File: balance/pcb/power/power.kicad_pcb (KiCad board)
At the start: 2 copper layers, 0 parts

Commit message: balance robot: power board
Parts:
- added A1: Pololu_Breakout_DRV8825, Module:Pololu_Breakout-16_15.2x20.3mm, F.Cu at (118.7, 53.6)
- added A2: Pololu_Breakout_DRV8825, Module:Pololu_Breakout-16_15.2x20.3mm, F.Cu at (181.3, 71.4)
- added J1: xt60, Connector_PinHeader_2.54mm:PinHeader_1x02_P2.54mm_Vertical, F.Cu at (148.7, 70.0)
- added J2: Conn_01x10_Male, Connector_PinHeader_2.54mm:PinHeader_1x10_P2.54mm_Vertical, F.Cu at (161.4, 55.0)
- added J3: Conn_01x04_Male, Connector_PinHeader_2.54mm:PinHeader_1x04_P2.54mm_Vertical, F.Cu at (110.0, 66.3)
- added J4: Conn_01x04_Male, Connector_PinHeader_2.54mm:PinHeader_1x04_P2.54mm_Vertical, F.Cu at (190.0, 58.7)
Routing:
- net /rb2: track 0.00 -> 8.65 mm
- net /rb1: track 0.00 -> 8.65 mm
- net /ra2: track 0.00 -> 8.65 mm
- net /ra1: track 0.00 -> 8.65 mm
- net /lb2: track 0.00 -> 8.65 mm
- net /lb1: track 0.00 -> 8.65 mm
- net /la2: track 0.00 -> 8.65 mm
- net /la1: track 0.00 -> 8.65 mm
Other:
- board outline added: 100 x 25 mm

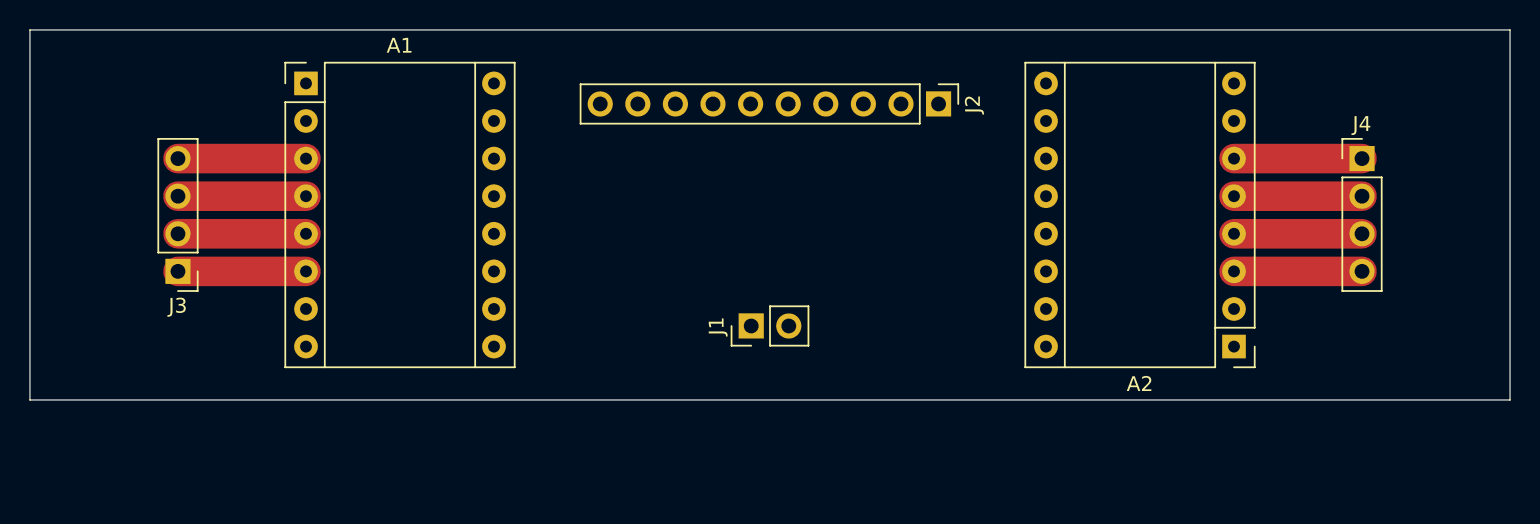
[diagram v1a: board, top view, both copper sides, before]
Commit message: balance robot: power board
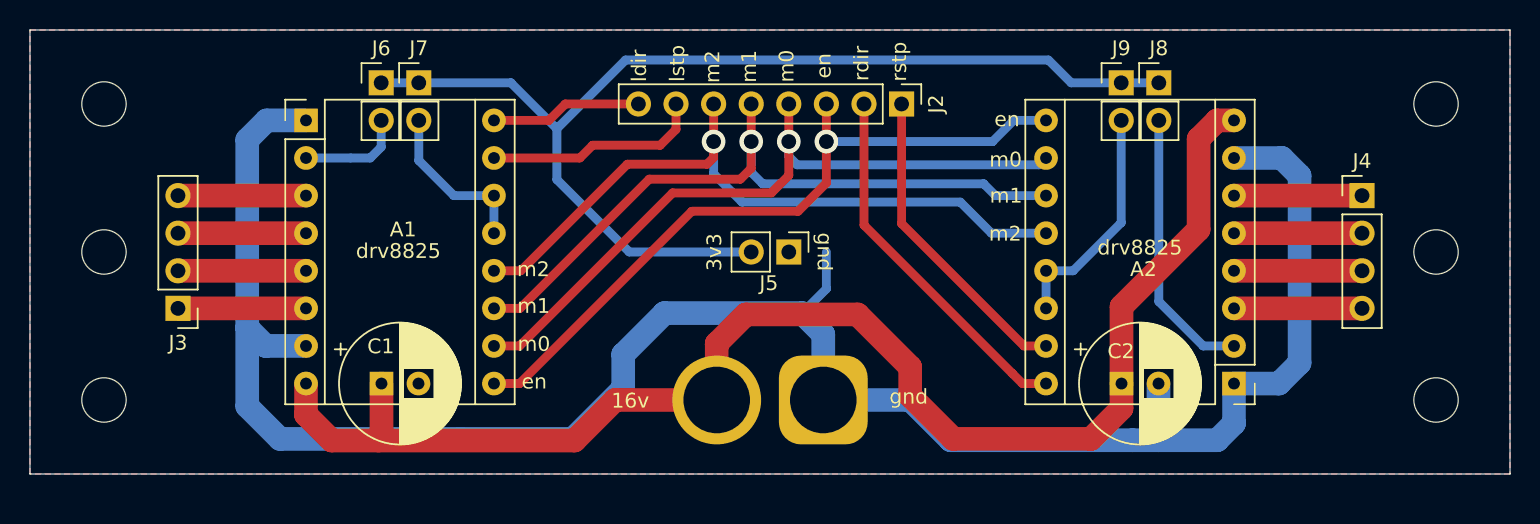
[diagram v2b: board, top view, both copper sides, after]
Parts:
- added C1: C, Capacitor_THT:CP_Radial_D8.0mm_P2.50mm, F.Cu at (123.8, 73.9)
- added C2: C, Capacitor_THT:CP_Radial_D8.0mm_P2.50mm, F.Cu at (173.8, 73.9)
- added J5: Conn_01x02_Male, Connector_PinHeader_2.54mm:PinHeader_1x02_P2.54mm_Vertical, F.Cu at (151.3, 65.0)
- added J6: Conn_01x02_Male, Connector_PinHeader_2.54mm:PinHeader_1x02_P2.54mm_Vertical, F.Cu at (123.7, 53.6)
- added J7: Conn_01x02_Male, Connector_PinHeader_2.54mm:PinHeader_1x02_P2.54mm_Vertical, F.Cu at (126.3, 53.6)
- added J8: Conn_01x02_Male, Connector_PinHeader_2.54mm:PinHeader_1x02_P2.54mm_Vertical, F.Cu at (176.3, 53.6)
- added J9: Conn_01x02_Male, Connector_PinHeader_2.54mm:PinHeader_1x02_P2.54mm_Vertical, F.Cu at (173.7, 53.6)
- J1: footprint Connector_PinHeader_2.54mm:PinHeader_1x02_P2.54mm_Vertical -> Connector_AMASS:AMASS_XT60-M_1x02_P7.20mm_Vertical; moved to B.Cu
- J2: value Conn_01x10_Male -> Conn_01x08_Male; footprint Connector_PinHeader_2.54mm:PinHeader_1x10_P2.54mm_Vertical -> Connector_PinHeader_2.54mm:PinHeader_1x08_P2.54mm_Vertical
- moved J1 6.98 mm to (153.6, 75.0), turned to 180 degrees
- moved A1 2.50 mm to (118.7, 56.1)
- moved A2 2.50 mm to (181.3, 73.9)
- moved J2 2.50 mm to (158.9, 55.0)
- moved J3 2.50 mm to (110.0, 68.8)
- moved J4 2.50 mm to (190.0, 61.2)
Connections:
- net Net-(A1-Pad8) renamed /12v
- A1 pad 13: /3v3 -> /lslp
- A1 pad 14: /3v3 -> /lslp
- A1 pad 2: /3v3 -> /lflt
- A2 pad 13: /3v3 -> /rslp
- A2 pad 14: /3v3 -> /rslp
- A2 pad 2: /3v3 -> /rflt
- J2 pad 1: /3v3 -> /rstep
- J2 pad 2: /gnd -> /rdir
- J2 pad 3: /m0 -> /en
- J2 pad 4: /m1 -> /m0
- J2 pad 5: /m2 -> /m1
- J2 pad 6: /en -> /m2
- J2 pad 7: /ldir -> /lstep
- J2 pad 8: /lstep -> /ldir
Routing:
- net GND: track 0.00 -> 140.0 mm
- net /12v: track 0.00 -> 96.1 mm
- net /3v3: track 0.00 -> 75.0 mm
- net /en: track 0.00 -> 48.8 mm, vias 0 -> 1
- net /m0: track 0.00 -> 48.3 mm, vias 0 -> 1
- net /m1: track 0.00 -> 48.3 mm, vias 0 -> 1
- net /m2: track 0.00 -> 47.9 mm, vias 0 -> 1
- net /rdir: track 0.00 -> 24.9 mm
- net /rstep: track 0.00 -> 21.3 mm
- net /rflt: track 0.00 -> 18.6 mm
- net /rslp: track 0.00 -> 15.9 mm
- net /lstep: track 0.00 -> 14.8 mm
- net /lslp: track 0.00 -> 11.3 mm
- net /ldir: track 0.00 -> 10.2 mm
- net /lflt: track 0.00 -> 7.19 mm
- added copper zone on B.Cu, net GND
- added copper zone on F.Cu, net GND
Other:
- board size 100 x 25 mm -> 100 x 30 mm
- board text added: "16v"
- board text added: "3v3"
- board text added: "drv8825"
- board text added: "en"
- board text added: "gnd"
- board text added: "ldir"
- board text added: "lstp"
- board text added: "m0"
- board text added: "m1"
- board text added: "m2"
- board text added: "rdir"
- board text added: "rstp"

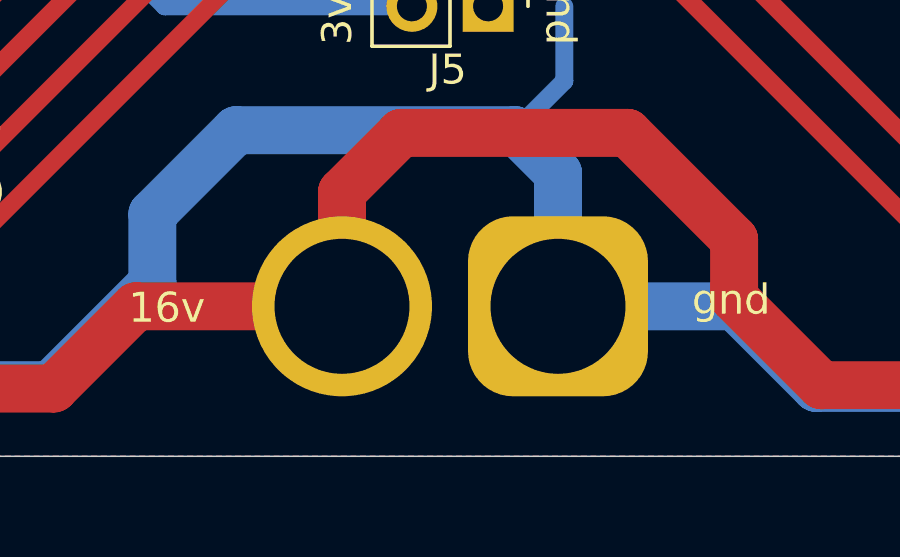
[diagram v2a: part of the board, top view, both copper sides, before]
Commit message: balance robot: cad,pcb
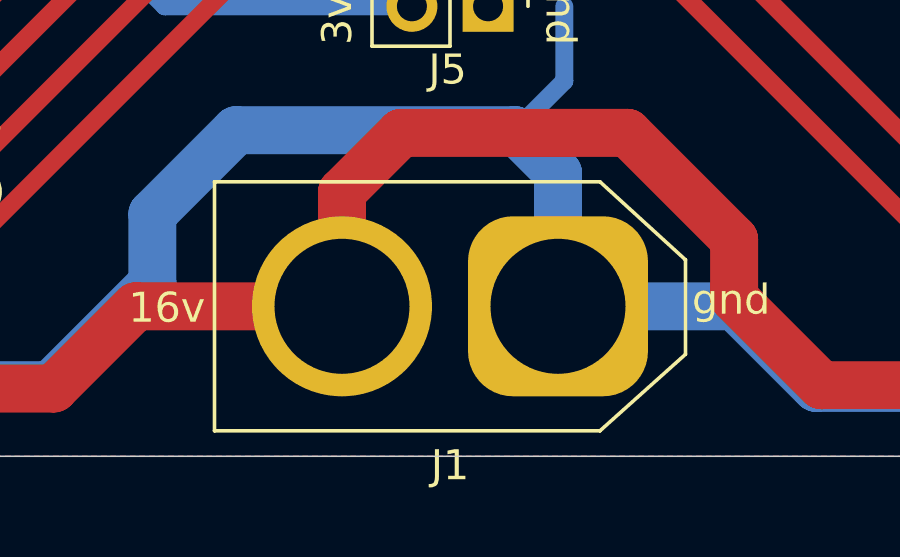
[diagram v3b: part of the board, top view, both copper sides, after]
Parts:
- J1: moved to F.Cu
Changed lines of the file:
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@@
+    )
+  )
+  (module "Connector_AMASS:AMASS_XT60-M_1x02_P7.20mm_Vertical" (layer "F.Cu")
+    (at 153.6 75 180)
+    (descr "AMASS female XT60, through hole, vertical, https://www.tme.eu/Document/2d152ced3b7a446066e6c419d84bb460/XT60%20SPEC.pdf")
+    (tags "XT60 female vertical")
+    (property "Sheet file" "/Users/ifbe/Desktop/code/ifbe/00/balance/pcb/power/power.kicad_sch")
+    (property "Sheet name" "")
+    (attr through_hole)
+    (fp_text reference "J1" (at 3.6 -5.3 180) (layer "F.SilkS")
+      (effects (font (size 1 1) (thickness 0.15)))
+    )
+    (fp_text value "xt60" (at 3.6 5.4) (layer "F.Fab")
+      (effects (font (size 1 1) (thickness 0.15)))
+    )
+    (fp_text user "${REFERENCE}" (at 3.6 0.05) (layer "F.Fab")
+      (effects (font (size 1 1) (thickness 0.15)))
+    )
+    (fp_line (start -4.25 1.55) (end -1.4 4.15) (layer "F.SilkS") (width 0.12))
+    (fp_line (start -4.25 -1.6) (end -4.25 1.55) (layer "F.SilkS") (width 0.12))
+    (fp_line (start -1.4 -4.15) (end -4.25 -1.6) (layer "F.SilkS") (width 0.12))
+    (fp_line (start 11.45 4.15) (end 11.45 -4.15) (layer "F.SilkS") (width 0.12))
+    (fp_line (start 11.45 -4.15) (end -1.4 -4.15) (layer "F.SilkS") (width 0.12))
+    (fp_line (start -1.4 4.15) (end 11.45 4.15) (layer "F.SilkS") (width 0.12))
+    (fp_line (start 11.85 -4.6) (end 11.85 4.6) (layer "F.CrtYd") (width 0.05))
+    (fp_line (start -4.65 -1.85) (end -1.6 -4.6) (layer "F.CrtYd") (width 0.05))
+    (fp_line (start -1.6 4.6) (end -4.65 1.85) (layer "F.CrtYd") (width 0.05))
+    (fp_line (start 11.85 4.6) (end -1.6 4.6) (layer "F.CrtYd") (width 0.05))
+    (fp_line (start -1.6 -4.6) (end 11.85 -4.6) (layer "F.CrtYd") (width 0.05))
+    (fp_line (start -4.65 1.85) (end -4.65 -1.85) (layer "F.CrtYd") (width 0.05))
+    (fp_line (start -4.15 1.55) (end -1.4 4.05) (layer "F.Fab") (width 0.12))
+    (fp_line (start 11.35 -4.05) (end -1.4 -4.05) (layer "F.Fab") (width 0.12))
+    (fp_line (start -1.4 4.05) (end 11.35 4.05) (layer "F.Fab") (width 0.12))
+    (fp_line (start -1.4 -4.05) (end -4.15 -1.55) (layer "F.Fab") (width 0.12))
+    (fp_line (start -4.15 -1.55) (end -4.15 1.55) (layer "F.Fab") (width 0.12))
+    (fp_line (start 11.35 4.05) (end 11.35 -4.05) (layer "F.Fab") (width 0.12))
+    (pad "1" thru_hole roundrect (at 0 0 180) (size 6 6) (drill 4.5) (layers *.Cu *.Mask) (roundrect_rratio 0.25)
+      (net 4 "GND") (pinfunction "Pin_1"))
+    (pad "2" thru_hole circle (at 7.2 0 180) (size 6 6) (drill 4.5) (layers *.Cu *.Mask)
+      (net 2 "/12v") (pinfunction "Pin_2"))
+    (model "${KISYS3DMOD}/Connector_AMASS.3dshapes/AMASS_XT60-M_1x02_P7.2mm_Vertical.wrl"
+      (offset (xyz 0 0 0))
+      (scale (xyz 1 1 1))
+      (rotate (xyz 0 0 0))
     )
   )
@@
       (offset (xyz 0 0 0))
       (scale (xyz 1 1 1))
-      (rotate (xyz 0 0 0))
-    )
-  )
-  (module "Connector_AMASS:AMASS_XT60-M_1x02_P7.20mm_Vertical" (layer "B.Cu")
-    (at 153.6 75 180)
-    (descr "AMASS female XT60, through hole, vertical, https://www.tme.eu/Document/2d152ced3b7a446066e6c419d84bb460/XT60%20SPEC.pdf")
-    (tags "XT60 female vertical")
-    (property "Sheet file" "/Users/ifbe/Desktop/code/ifbe/00/balance/pcb/power/power.kicad_sch")
-    (property "Sheet name" "")
-    (attr through_hole)
-    (fp_text reference "J1" (at 3.6 5.3 180) (layer "B.SilkS")
-      (effects (font (size 1 1) (thickness 0.15)) (justify mirror))
-    )
-    (fp_text value "xt60" (at 3.6 -5.4) (layer "B.Fab")
-      (effects (font (size 1 1) (thickness 0.15)) (justify mirror))
-    )
-    (fp_text user "${REFERENCE}" (at 3.6 -0.05) (layer "B.Fab")
-      (effects (font (size 1 1) (thickness 0.15)) (justify mirror))
-    )
-    (fp_line (start -4.25 -1.55) (end -1.4 -4.15) (layer "B.SilkS") (width 0.12))
-    (fp_line (start -4.25 1.6) (end -4.25 -1.55) (layer "B.SilkS") (width 0.12))
-    (fp_line (start -1.4 4.15) (end -4.25 1.6) (layer "B.SilkS") (width 0.12))
-    (fp_line (start 11.45 -4.15) (end 11.45 4.15) (layer "B.SilkS") (width 0.12))
-    (fp_line (start 11.45 4.15) (end -1.4 4.15) (layer "B.SilkS") (width 0.12))
-    (fp_line (start -1.4 -4.15) (end 11.45 -4.15) (layer "B.SilkS") (width 0.12))
-    (fp_line (start 11.85 4.6) (end 11.85 -4.6) (layer "B.CrtYd") (width 0.05))
-    (fp_line (start -4.65 1.85) (end -1.6 4.6) (layer "B.CrtYd") (width 0.05))
-    (fp_line (start -1.6 -4.6) (end -4.65 -1.85) (layer "B.CrtYd") (width 0.05))
-    (fp_line (start 11.85 -4.6) (end -1.6 -4.6) (layer "B.CrtYd") (width 0.05))
-    (fp_line (start -1.6 4.6) (end 11.85 4.6) (layer "B.CrtYd") (width 0.05))
-    (fp_line (start -4.65 -1.85) (end -4.65 1.85) (layer "B.CrtYd") (width 0.05))
-    (fp_line (start -4.15 -1.55) (end -1.4 -4.05) (layer "B.Fab") (width 0.12))
-    (fp_line (start 11.35 4.05) (end -1.4 4.05) (layer "B.Fab") (width 0.12))
-    (fp_line (start -1.4 -4.05) (end 11.35 -4.05) (layer "B.Fab") (width 0.12))
-    (fp_line (start -1.4 4.05) (end -4.15 1.55) (layer "B.Fab") (width 0.12))
-    (fp_line (start -4.15 1.55) (end -4.15 -1.55) (layer "B.Fab") (width 0.12))
-    (fp_line (start 11.35 -4.05) (end 11.35 4.05) (layer "B.Fab") (width 0.12))
-    (pad "1" thru_hole roundrect (at 0 0 180) (size 6 6) (drill 4.5) (layers *.Cu *.Mask) (roundrect_rratio 0.25)
-      (net 4 "GND") (pinfunction "Pin_1"))
-    (pad "2" thru_hole circle (at 7.2 0 180) (size 6 6) (drill 4.5) (layers *.Cu *.Mask)
-      (net 2 "/12v") (pinfunction "Pin_2"))
-    (model "${KISYS3DMOD}/Connector_AMASS.3dshapes/AMASS_XT60-M_1x02_P7.2mm_Vertical.wrl"
-      (offset (xyz 0 0 0))
-      (scale (xyz 1 1 1))
